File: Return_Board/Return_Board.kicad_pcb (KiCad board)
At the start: 2 copper layers, 25.2 x 43.5 mm, 9 parts, among them J1 Conn_01x02_Pin, J2 Conn_01x06_Pin, U1 74HC14, U2 LM317LZ

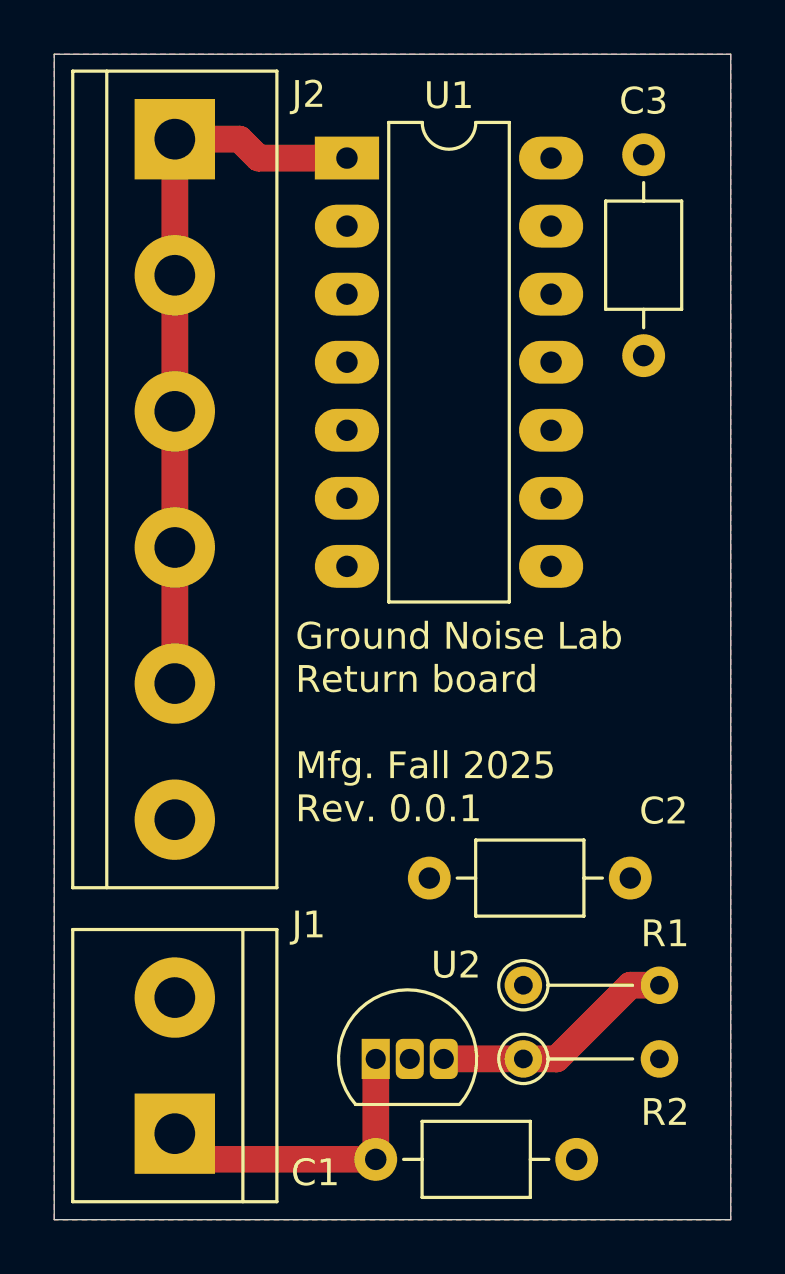
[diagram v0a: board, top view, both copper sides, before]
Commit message: Return board version 0.0.2; updates in README
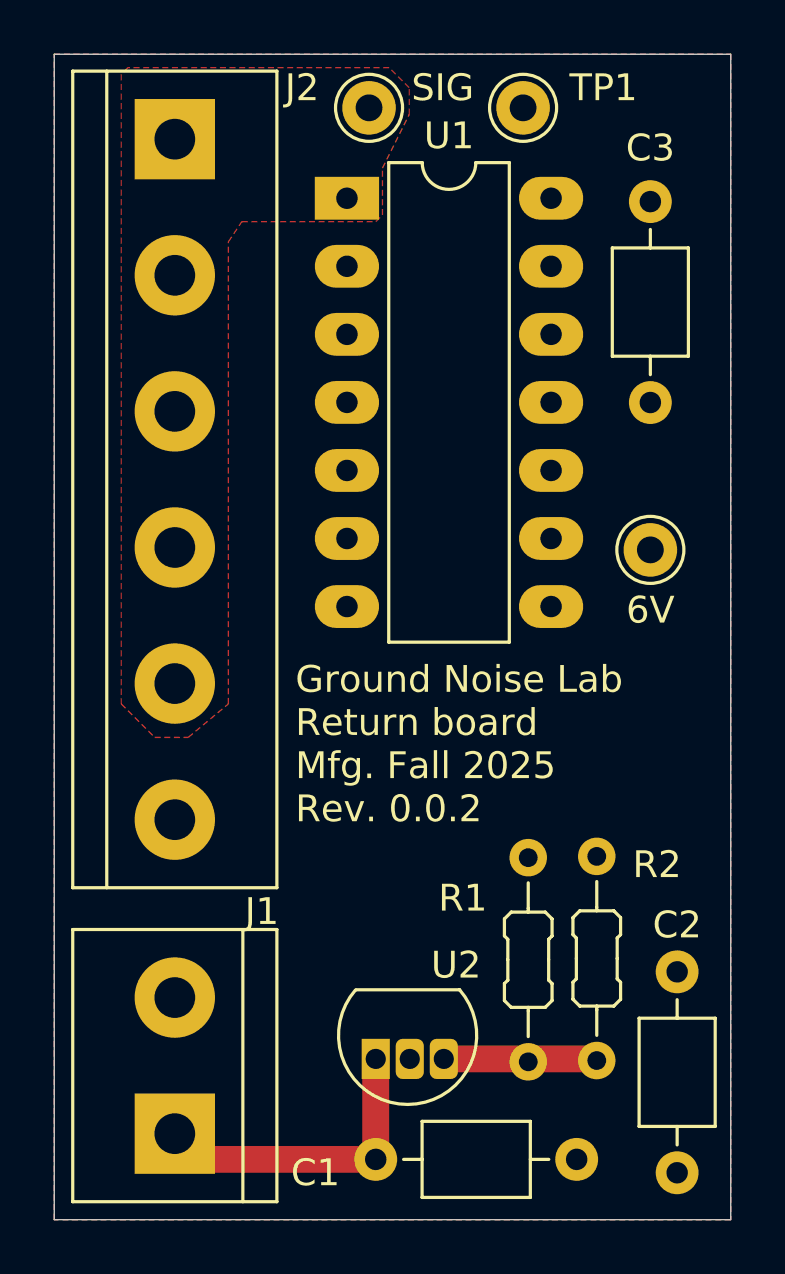
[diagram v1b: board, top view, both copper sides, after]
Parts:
- added 6V: 6 V, Connector_Pin:Pin_D1.0mm_L10.0mm, F.Cu at (154.5, 86.0)
- added SIG: SIG, Connector_Pin:Pin_D1.0mm_L10.0mm, F.Cu at (144.0, 69.5)
- added TP1: GND, Connector_Pin:Pin_D1.0mm_L10.0mm, F.Cu at (149.8, 69.5)
- R1: value 1k -> 240; footprint PCM_Resistor_THT_AKL:R_Axial_DIN0204_L3.6mm_D1.6mm_P5.08mm_Vertical -> PCM_Resistor_THT_AKL:R_Axial_DIN0204_L3.6mm_D1.6mm_P7.62mm_Horizontal
- R2: value 3k6 -> 910; footprint PCM_Resistor_THT_AKL:R_Axial_DIN0204_L3.6mm_D1.6mm_P5.08mm_Vertical -> PCM_Resistor_THT_AKL:R_Axial_DIN0204_L3.6mm_D1.6mm_P7.62mm_Horizontal
- moved C2 9.89 mm to (155.5, 101.8), turned to -90 degrees
- moved R1 4.77 mm to (149.9, 97.5), turned to -90 degrees
- moved R2 2.74 mm to (152.5, 105.1), turned to 90 degrees
- moved C3 1.77 mm to (154.5, 73.0)
- moved U1 1.50 mm to (143.2, 72.9)
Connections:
- U1 pad 10: GND -> unconnected-(U1-Pad10)
- U1 pad 12: GND -> unconnected-(U1-Pad12)
- U1 pad 4: GND -> unconnected-(U1-Pad4)
- U1 pad 6: GND -> unconnected-(U1-Pad6)
- U1 pad 8: GND -> unconnected-(U1-Pad8)
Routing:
- net /SIG_Out: track 27.0 -> 0.00 mm
- net /LDO_ADJ: track 9.19 -> 5.73 mm
- added copper zone on F.Cu, net /SIG_Out
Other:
- board text added: "Ground Noise Lab Return board Mfg. Fall 2025 Rev. 0.0.2"
- board text removed: "Ground Noise Lab Return board Mfg. Fall 2025 Rev. 0.0.1"
